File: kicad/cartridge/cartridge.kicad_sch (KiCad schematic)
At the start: 12 parts, among them J1 Card edge (87715-9106 mate), U1 ATF22V10C-10PU, U2 AT28C256-15PU, U3 AT28C256-15PU, U4 AS7C256C-15PCN, U5 AS7C256C-15PCN

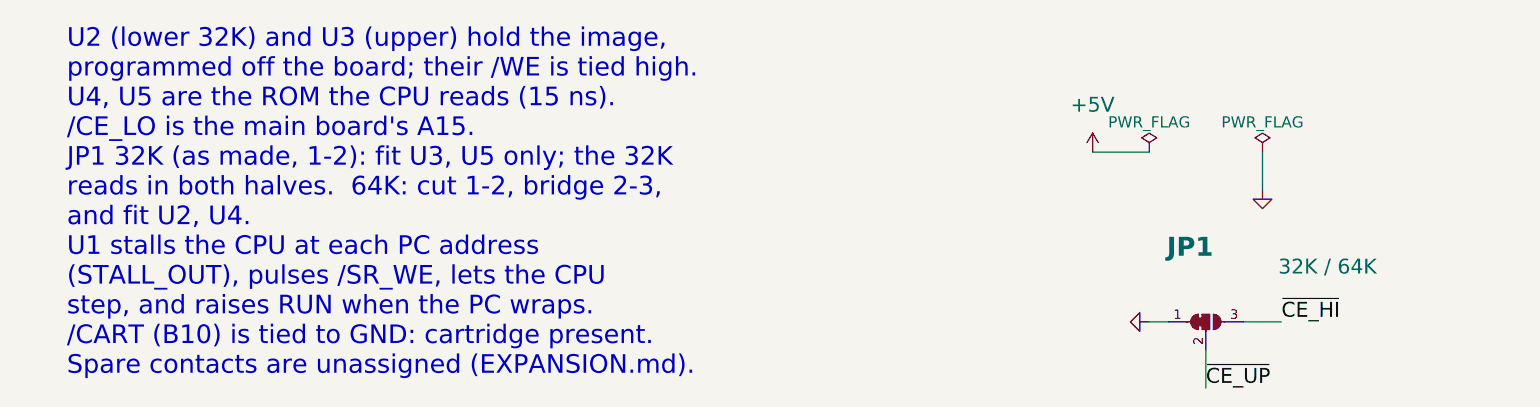
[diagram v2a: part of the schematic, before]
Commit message: Cartridge JP1: as-made bridge is 64K (development), 32K by cutting it
Co-Authored-By: Claude Opus 5.5 (1M context) <noreply@anthropic.com>
Claude-Session: https://claude.ai/code/session_01PNJoPfzmo1tu8EorCrua96
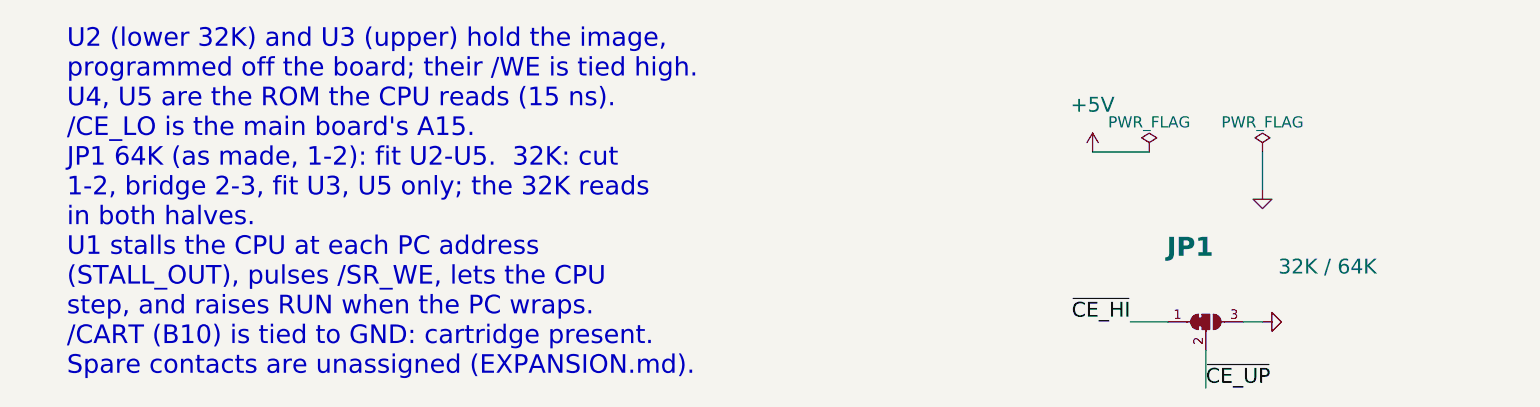
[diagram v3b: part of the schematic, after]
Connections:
- net GND: now also JP1.3 (B); no longer JP1.1 (A)
- net ~{CE_HI}: now also JP1.1 (A); no longer JP1.3 (B)
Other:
- note added: "1-2, bridge 2-3, fit U3, U5 only; the 32K reads"
- note added: "JP1 64K (as made, 1-2): fit U2-U5. 32K: cut"
- note added: "in both halves."
- note removed: "JP1 32K (as made, 1-2): fit U3, U5 only; the 32K"
- note removed: "and fit U2, U4."
- note removed: "reads in both halves. 64K: cut 1-2, bridge 2-3,"
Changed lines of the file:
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@@
   (symbol (lib_id "power:GND") (at 342.9 161.29 0) (unit 1) (in_bom yes) (on_board yes) (dnp no) (property "Reference" "#PWR0129" (at 342.9 161.29 0) (effects (font (size 1.27 1.27)) hide)) (property "Value" "GND" (at 342.9 167.64 0) (effects (font (size 2 2)) hide)) (property "Footprint" "" (at 342.9 161.29 0) (effects (font (size 1.27 1.27)) hide)) (property "Datasheet" "" (at 342.9 161.29 0) (effects (font (size 1.27 1.27)) hide)) (pin "1") (instances (project "cartridge" (path "/58e6aaf0-b096-58ec-a49b-041f90960c95" (reference "#PWR0129") (unit 1)))))
   (symbol (lib_id "placard_std:C") (at 342.9 157.48 0) (unit 1) (in_bom yes) (on_board yes) (dnp no) (property "Reference" "C5" (at 344.9 156.98 0) (effects (font (size 2.54 2.54) bold) (justify left bottom))) (property "Value" "100n" (at 344.9 160.08 0) (effects (font (size 2 2)) (justify left top))) (property "Footprint" "Capacitor_THT:C_Disc_D5.0mm_W2.5mm_P5.00mm" (at 342.9 157.48 0) (effects (font (size 1.27 1.27)) hide)) (property "Datasheet" "~" (at 342.9 157.48 0) (effects (font (size 1.27 1.27)) hide)) (pin "1") (pin "2") (instances (project "cartridge" (path "/58e6aaf0-b096-58ec-a49b-041f90960c95" (reference "C5") (unit 1)))))
-  (wire (pts (xy 170.18 228.6) (xy 167.64 228.6)) (stroke (width 0) (type default)))
-  (symbol (lib_id "power:GND") (at 167.64 228.6 270) (unit 1) (in_bom yes) (on_board yes) (dnp no) (property "Reference" "#PWR0130" (at 167.64 228.6 0) (effects (font (size 1.27 1.27)) hide)) (property "Value" "GND" (at 159.29 228.6 90) (effects (font (size 2 2)) hide)) (property "Footprint" "" (at 167.64 228.6 0) (effects (font (size 1.27 1.27)) hide)) (property "Datasheet" "" (at 167.64 228.6 0) (effects (font (size 1.27 1.27)) hide)) (pin "1") (instances (project "cartridge" (path "/58e6aaf0-b096-58ec-a49b-041f90960c95" (reference "#PWR0130") (unit 1)))))
+  (wire (pts (xy 180.34 228.6) (xy 182.88 228.6)) (stroke (width 0) (type default)))
+  (symbol (lib_id "power:GND") (at 182.88 228.6 90) (unit 1) (in_bom yes) (on_board yes) (dnp no) (property "Reference" "#PWR0130" (at 182.88 228.6 0) (effects (font (size 1.27 1.27)) hide)) (property "Value" "GND" (at 191.23 228.6 90) (effects (font (size 2 2)) hide)) (property "Footprint" "" (at 182.88 228.6 0) (effects (font (size 1.27 1.27)) hide)) (property "Datasheet" "" (at 182.88 228.6 0) (effects (font (size 1.27 1.27)) hide)) (pin "1") (instances (project "cartridge" (path "/58e6aaf0-b096-58ec-a49b-041f90960c95" (reference "#PWR0130") (unit 1)))))
   (symbol (lib_id "Jumper:SolderJumper_3_Bridged12") (at 175.26 228.6 0) (unit 1) (in_bom yes) (on_board yes) (dnp no) (property "Reference" "JP1" (at 170 220 0) (effects (font (size 2.54 2.54) bold) (justify left bottom))) (property "Value" "32K / 64K" (at 185 220 0) (effects (font (size 2 2)) (justify left top))) (property "Footprint" "Jumper:SolderJumper-3_P1.3mm_Bridged12_RoundedPad1.0x1.5mm_NumberLabels" (at 175.26 228.6 0) (effects (font (size 1.27 1.27)) hide)) (property "Datasheet" "~" (at 175.26 228.6 0) (effects (font (size 1.27 1.27)) hide)) (pin "1") (pin "2") (pin "3") (instances (project "cartridge" (path "/58e6aaf0-b096-58ec-a49b-041f90960c95" (reference "JP1") (unit 1)))))
   (text "U2 (lower 32K) and U3 (upper) hold the image," (at 22 192 0) (effects (font (size 2.5 2.5)) (justify left bottom)))
@@
   (text "U4, U5 are the ROM the CPU reads (15 ns)." (at 22 200 0) (effects (font (size 2.5 2.5)) (justify left bottom)))
   (text "/CE_LO is the main board's A15." (at 22 204 0) (effects (font (size 2.5 2.5)) (justify left bottom)))
-  (text "JP1 32K (as made, 1-2): fit U3, U5 only; the 32K" (at 22 208 0) (effects (font (size 2.5 2.5)) (justify left bottom)))
-  (text "reads in both halves.  64K: cut 1-2, bridge 2-3," (at 22 212 0) (effects (font (size 2.5 2.5)) (justify left bottom)))
-  (text "and fit U2, U4." (at 22 216 0) (effects (font (size 2.5 2.5)) (justify left bottom)))
+  (text "JP1 64K (as made, 1-2): fit U2-U5.  32K: cut" (at 22 208 0) (effects (font (size 2.5 2.5)) (justify left bottom)))
+  (text "1-2, bridge 2-3, fit U3, U5 only; the 32K reads" (at 22 212 0) (effects (font (size 2.5 2.5)) (justify left bottom)))
+  (text "in both halves." (at 22 216 0) (effects (font (size 2.5 2.5)) (justify left bottom)))
   (text "U1 stalls the CPU at each PC address" (at 22 220 0) (effects (font (size 2.5 2.5)) (justify left bottom)))
   (text "(STALL_OUT), pulses /SR_WE, lets the CPU" (at 22 224 0) (effects (font (size 2.5 2.5)) (justify left bottom)))
@@
   (bus (pts (xy 384.81 184.15) (xy 384.81 186.69)) (stroke (width 0) (type default)))
   (bus (pts (xy 384.81 186.69) (xy 384.81 189.23)) (stroke (width 0) (type default)))
+  (wire (pts (xy 170.18 228.6) (xy 165.1 228.6)) (stroke (width 0) (type default)))
+  (label "~{CE_HI}" (at 165.1 228.6 180) (fields_autoplaced) (effects (font (size 2 2)) (justify right bottom)))
   (wire (pts (xy 175.26 232.41) (xy 175.26 237.49)) (stroke (width 0) (type default)))
   (label "~{CE_UP}" (at 175.26 237.49 0) (fields_autoplaced) (effects (font (size 2 2)) (justify left bottom)))
-  (wire (pts (xy 180.34 228.6) (xy 185.42 228.6)) (stroke (width 0) (type default)))
-  (label "~{CE_HI}" (at 185.42 228.6 0) (fields_autoplaced) (effects (font (size 2 2)) (justify left bottom)))
   (label "~{CE_LO}" (at 52.07 119.38 180) (fields_autoplaced) (effects (font (size 2 2)) (justify right bottom)))
   (label "~{CE_HI}" (at 52.07 121.92 180) (fields_autoplaced) (effects (font (size 2 2)) (justify right bottom)))

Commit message: Bill of materials for the main board, cartridge and keyboard
Manufacturer and MPN fields on every schematic part (empty where none is
chosen), set from an MPN table in gen_kicad_schematic.py; net tie, cartridge
edge fingers and solder jumper excluded from the BOM.  gen_bom.py groups the
parts by part number into docs/BOM.md and docs/BOM.csv, adding sockets,
shunts, keyboard LEDs, keycaps, stabilizers and the keyboard ribbon cable.

Co-Authored-By: Claude Opus 5.5 (1M context) <noreply@anthropic.com>
Claude-Session: https://claude.ai/code/session_018iEnPngycbxX6Tt4Wzp3zN
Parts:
- J1, JP1: now left out of the parts list
- U1: MPN (none) -> ATF22V10C-10PU; Manufacturer (none) -> Microchip
- U2, U3: MPN (none) -> AT28C256-15PU; Manufacturer (none) -> Microchip
- U4, U5: MPN (none) -> AS7C256C-15PCN; Manufacturer (none) -> Alliance Memory

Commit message: Part numbers for the remaining parts; J6 Tensility 54-00174; optional J1 and J9-J12
Every schematic part gets Manufacturer/MPN: Yageo MFR-25 resistors by value,
Bourns 4609X networks, KEMET/TDK ceramics, Panasonic FR electrolytics, ECS
oscillator, Assmann VGA, Sullins headers, Wurth box header, Cherry switches.
Sockets get On Shore numbers (0.3" 24/28-pin are ED241DT/ED281DT; ED28DT is
0.6"). J6 becomes the Tensility 54-00174 TRRS jack with a footprint drawn
from its datasheet. Digi-Key prices from Justin for the oscillator, VGA and
audio jack. The expansion slot sockets and the keyboard header are optional,
with a BOM total without them.

Co-Authored-By: Claude Opus 5.5 (1M context) <noreply@anthropic.com>
Claude-Session: https://claude.ai/code/session_01L9AkLuEg13EebxDmgXsaEp
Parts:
- C1, C2, C3, C4, C5: MPN (none) -> C320C104K5R5TA; Manufacturer (none) -> KEMET

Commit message: Every PLD is an ATF22V10C-7PX (one part number)
Justin: switch the seven main-board -10PU PLDs (Branch, PC x2, H, V,
color decoder, audio slot) and the cartridge loader to the -7PX, for one
part number to buy, program and kit (.52 more per main board). Symbols,
schematics, PDFs, BOM, docs and PLD comments updated; CHIPS.md keeps the
grade each PLD could use.

Co-Authored-By: Claude Opus 5.5 (1M context) <noreply@anthropic.com>
Claude-Session: https://claude.ai/code/session_01JnVuvUvdWezUUU6Sgmg16H
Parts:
- U1: value ATF22V10C-10PU -> ATF22V10C-7PX; MPN ATF22V10C-10PU -> ATF22V10C-7PX
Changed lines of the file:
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@@
   (wire (pts (xy 175.26 172.72) (xy 175.26 175.26)) (stroke (width 0) (type default)))
   (symbol (lib_id "power:GND") (at 175.26 175.26 0) (unit 1) (in_bom yes) (on_board yes) (dnp no) (property "Reference" "#PWR0105" (at 175.26 175.26 0) (effects (font (size 1.27 1.27)) hide)) (property "Value" "GND" (at 175.26 181.61 0) (effects (font (size 2 2)) hide)) (property "Footprint" "" (at 175.26 175.26 0) (effects (font (size 1.27 1.27)) hide)) (property "Datasheet" "" (at 175.26 175.26 0) (effects (font (size 1.27 1.27)) hide)) (pin "1") (instances (project "cartridge" (path "/58e6aaf0-b096-58ec-a49b-041f90960c95" (reference "#PWR0105") (unit 1)))))
-  (symbol (lib_id "placard:ATF22V10C_CART") (at 175.26 134.62 0) (unit 1) (in_bom yes) (on_board yes) (dnp no) (property "Reference" "U1" (at 159.258 95.02 0) (effects (font (size 2.54 2.54) bold) (justify left bottom))) (property "Value" "ATF22V10C-10PU" (at 159.258 176.72 0) (effects (font (size 2 2)) (justify left top))) (property "Function" "Loader PLD" (at 159.258 180.12 0) (effects (font (size 2.54 2.54) bold) (justify left top))) (property "Footprint" "Package_DIP:DIP-24_W7.62mm" (at 175.26 134.62 0) (effects (font (size 1.27 1.27)) hide)) (property "Datasheet" "https://ww1.microchip.com/downloads/en/DeviceDoc/doc0735.pdf" (at 175.26 134.62 0) (effects (font (size 1.27 1.27)) hide)) (property "Manufacturer" "Microchip" (at 175.26 134.62 0) (effects (font (size 1.27 1.27)) hide)) (property "MPN" "ATF22V10C-10PU" (at 175.26 134.62 0) (effects (font (size 1.27 1.27)) hide)) (property "PLD" "ATF22V10_CART.pld" (at 175.26 134.62 0) (effects (font (size 1.27 1.27)) hide)) (pin "1") (pin "3") (pin "4") (pin "5") (pin "23") (pin "22") (pin "2") (pin "6") (pin "7") (pin "8") (pin "9") (pin "10") (pin "11") (pin "13") (pin "14") (pin "15") (pin "16") (pin "17") (pin "18") (pin "21") (pin "20") (pin "19") (pin "24") (pin "12") (instances (project "cartridge" (path "/58e6aaf0-b096-58ec-a49b-041f90960c95" (reference "U1") (unit 1)))))
+  (symbol (lib_id "placard:ATF22V10C_CART") (at 175.26 134.62 0) (unit 1) (in_bom yes) (on_board yes) (dnp no) (property "Reference" "U1" (at 159.258 95.02 0) (effects (font (size 2.54 2.54) bold) (justify left bottom))) (property "Value" "ATF22V10C-7PX" (at 159.258 176.72 0) (effects (font (size 2 2)) (justify left top))) (property "Function" "Loader PLD" (at 159.258 180.12 0) (effects (font (size 2.54 2.54) bold) (justify left top))) (property "Footprint" "Package_DIP:DIP-24_W7.62mm" (at 175.26 134.62 0) (effects (font (size 1.27 1.27)) hide)) (property "Datasheet" "https://ww1.microchip.com/downloads/en/DeviceDoc/doc0735.pdf" (at 175.26 134.62 0) (effects (font (size 1.27 1.27)) hide)) (property "Manufacturer" "Microchip" (at 175.26 134.62 0) (effects (font (size 1.27 1.27)) hide)) (property "MPN" "ATF22V10C-7PX" (at 175.26 134.62 0) (effects (font (size 1.27 1.27)) hide)) (property "PLD" "ATF22V10_CART.pld" (at 175.26 134.62 0) (effects (font (size 1.27 1.27)) hide)) (pin "1") (pin "3") (pin "4") (pin "5") (pin "23") (pin "22") (pin "2") (pin "6") (pin "7") (pin "8") (pin "9") (pin "10") (pin "11") (pin "13") (pin "14") (pin "15") (pin "16") (pin "17") (pin "18") (pin "21") (pin "20") (pin "19") (pin "24") (pin "12") (instances (project "cartridge" (path "/58e6aaf0-b096-58ec-a49b-041f90960c95" (reference "U1") (unit 1)))))
   (wire (pts (xy 107.95 101.6) (xy 152.4 101.6)) (stroke (width 0) (type default)))
   (wire (pts (xy 107.95 106.68) (xy 152.4 106.68)) (stroke (width 0) (type default)))
